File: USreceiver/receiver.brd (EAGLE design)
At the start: 114 x 77.5 mm, 53 parts, among them U1 LMP7712MM, U2 LMP7712MM, U3 LMP7712MM, U4 LMP7712MM, U5 LM1117MP-3.3

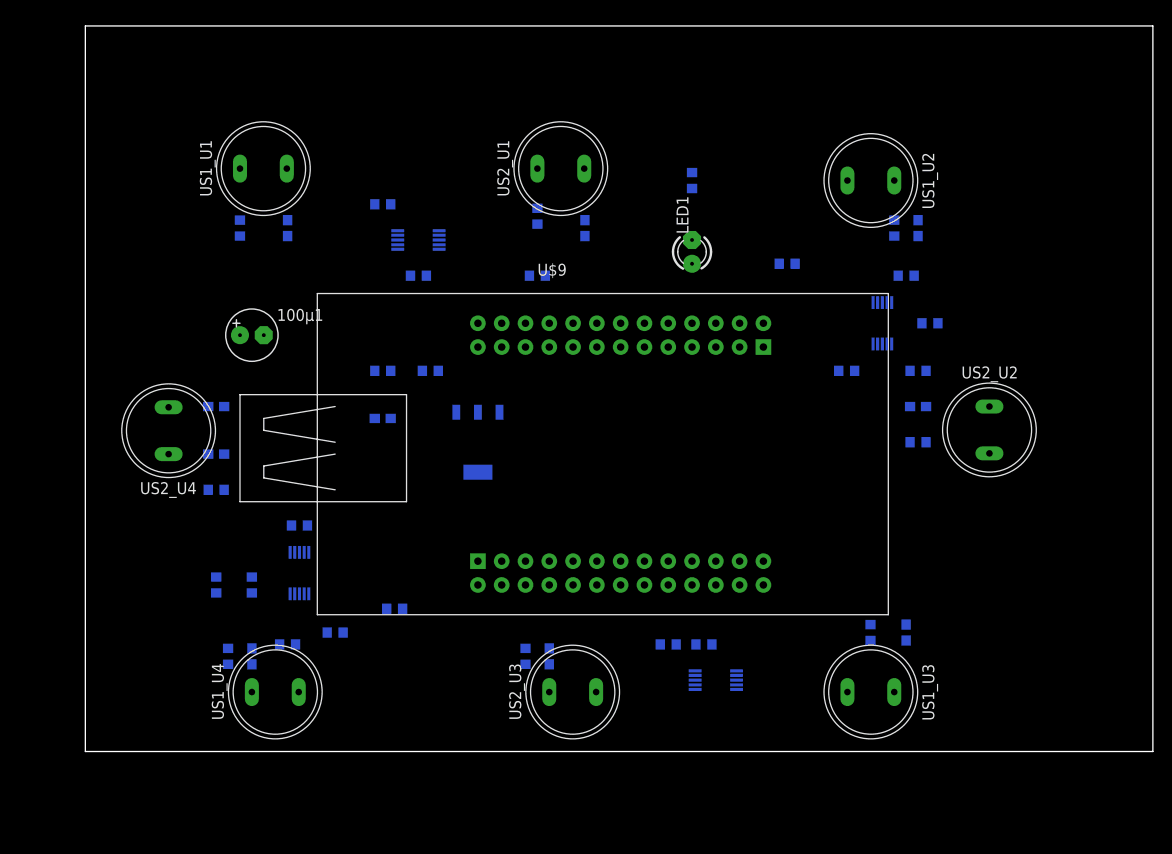
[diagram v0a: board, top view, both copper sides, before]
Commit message: Board finished
Board design is finished, pictures are exported. Ready to be sent in
fab.
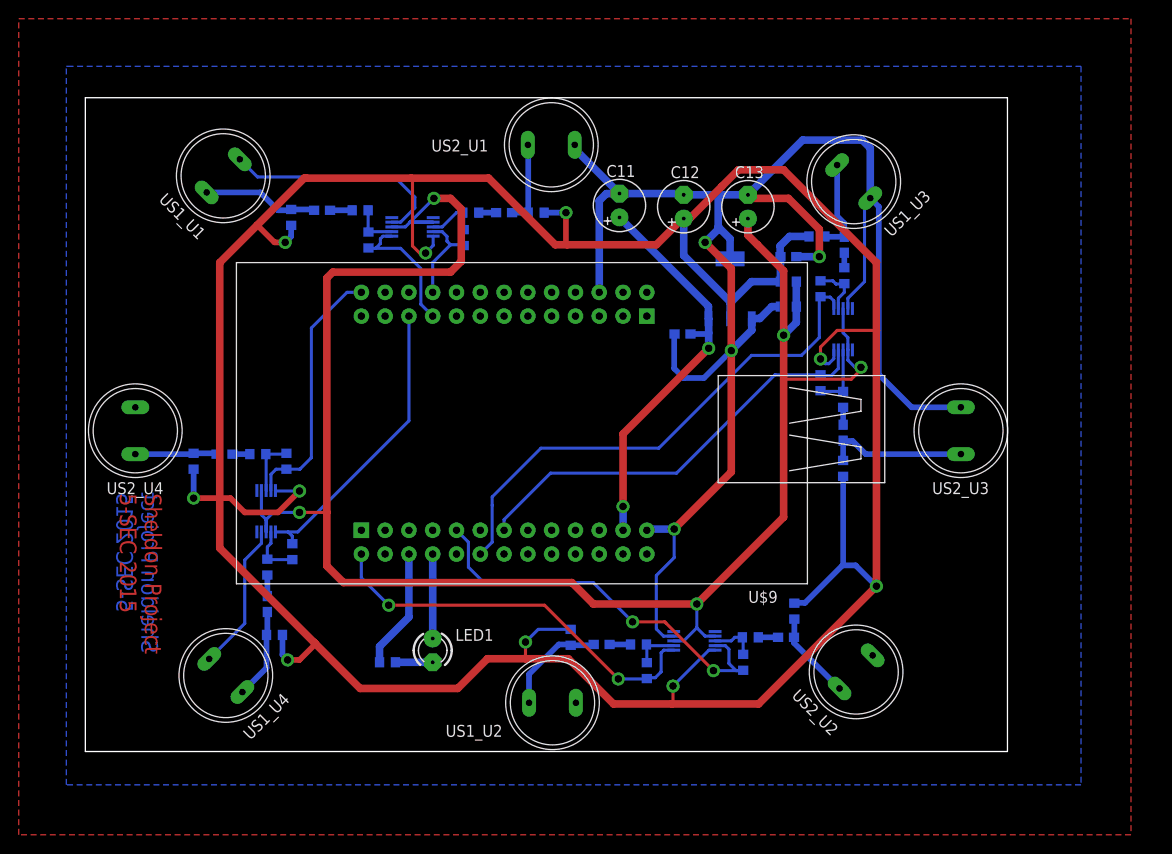
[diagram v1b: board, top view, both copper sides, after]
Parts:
- removed 100µ1: (no value), @Club_passif:E2,5-6
- added C11: 100µ, @Club_passif:E2,5-6
- added C12, C13: 2.2µ, @Club_passif:E2,5-6
- R1, R12, R15, R17, R19, R21, R4, R9: value (none) -> 1k
- R10, R14, R2, R23, R24, R25, R26, R8: value (none) -> 100k
- moved US1_U2 68.0 mm to (47.4, 5.21), turned to 90 degrees
- moved R24 63.5 mm to (78.5, 49.4), turned to 270 degrees
- moved R27 60.8 mm to (32.3, 9.53), turned to 0 degrees
- moved R15 59.7 mm to (81.0, 50.8), turned to 270 degrees
- moved US1_U3 56.6 mm to (80.3, 62.6), turned to 45 degrees
- moved C1 55.8 mm to (55.1, 11.4), turned to 180 degrees
- moved R11 55.7 mm to (51.8, 12.2), turned to 90 degrees
- moved LED1 50.8 mm to (37.1, 10.8), turned to 270 degrees
- moved US2_U3 50.8 mm to (93.5, 31.8), turned to 180 degrees
- moved C10 50.4 mm to (63.8, 44.6)
- moved C2 46.6 mm to (75.1, 52.8), turned to 180 degrees
- moved R9 46.3 mm to (59.1, 11.4), turned to 180 degrees
- moved R1 45.9 mm to (29.3, 57.8), turned to 180 degrees
- moved R10 44.8 mm to (70.2, 9.53), turned to 90 degrees
- moved R7 43.8 mm to (75.1, 47.5)
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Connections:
- net +3V3: now also C12.+
- net +5V: now also C11.+; no longer 100µ1.+
- net GND: now also C11.-, C12.-, C13.-; no longer 100µ1.-
- net VCC/2: now also C13.+
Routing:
- net +3V3: track 0.00 -> 355.2 mm, vias 0 -> 10
- net GND: track 0.00 -> 244.8 mm, vias 0 -> 4
- net VCC/2: track 0.00 -> 196.6 mm, vias 0 -> 5
- net S5: track 0.00 -> 55.4 mm
- net S6: track 0.00 -> 45.6 mm
- net S4: track 0.00 -> 43.4 mm, vias 0 -> 2
- net +5V: track 0.00 -> 43.1 mm, vias 0 -> 2
- net S3: track 0.00 -> 42.8 mm, vias 0 -> 2
- net S7: track 0.00 -> 31.8 mm
- net S8: track 0.00 -> 27.5 mm
- net N$11: track 0.00 -> 15.3 mm
- net S1: track 0.00 -> 14.7 mm
- net N$3: track 0.00 -> 12.3 mm
- net N$1: track 0.00 -> 11.3 mm
- net N$9: track 0.00 -> 10.1 mm
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- added copper zone on layer 1, net GND
- added copper zone on layer 16, net GND
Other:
- board size 114 x 77.5 mm -> 98.4 x 69.8 mm
- board text added: "Sheldon Project 5-SEC 2015"
